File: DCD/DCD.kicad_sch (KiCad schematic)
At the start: 0 parts

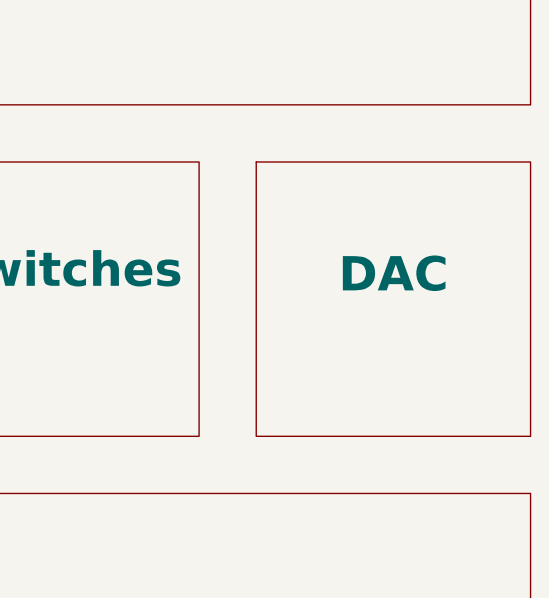
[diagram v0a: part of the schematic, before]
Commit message: DAC schematic with opamp and top level added
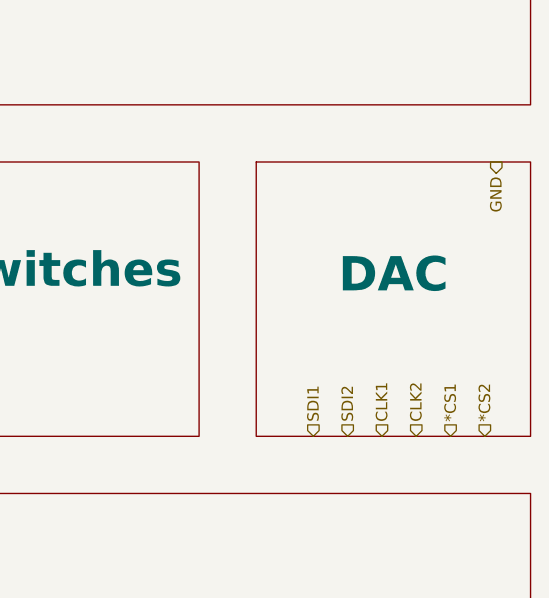
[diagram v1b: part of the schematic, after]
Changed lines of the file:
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@@
 	(generator_version "9.0")
 	(paper "A4")
+	(hierarchical_label "*CS2"
+		(shape input)
+		(at 177.8 109.22 90)
+		(effects
+			(font
+				(size 1.27 1.27)
+			)
+			(justify left)
+		)
+	)
+	(hierarchical_label "CLK2"
+		(shape input)
+		(at 170.18 109.22 90)
+		(effects
+			(font
+				(size 1.27 1.27)
+			)
+			(justify left)
+		)
+	)
+	(hierarchical_label "CLK1"
+		(shape input)
+		(at 166.37 109.22 90)
+		(effects
+			(font
+				(size 1.27 1.27)
+			)
+			(justify left)
+		)
+	)
+	(hierarchical_label "SDI1"
+		(shape input)
+		(at 158.75 109.22 90)
+		(effects
+			(font
+				(size 1.27 1.27)
+			)
+			(justify left)
+		)
+	)
+	(hierarchical_label "GND"
+		(shape output)
+		(at 179.07 78.74 270)
+		(effects
+			(font
+				(size 1.27 1.27)
+			)
+			(justify right)
+		)
+	)
+	(hierarchical_label "*CS1"
+		(shape input)
+		(at 173.99 109.22 90)
+		(effects
+			(font
+				(size 1.27 1.27)
+			)
+			(justify left)
+		)
+	)
+	(hierarchical_label "SDI2"
+		(shape input)
+		(at 162.56 109.22 90)
+		(effects
+			(font
+				(size 1.27 1.27)
+			)
+			(justify left)
+		)
+	)
 	(sheet
 		(at 152.4 78.74)

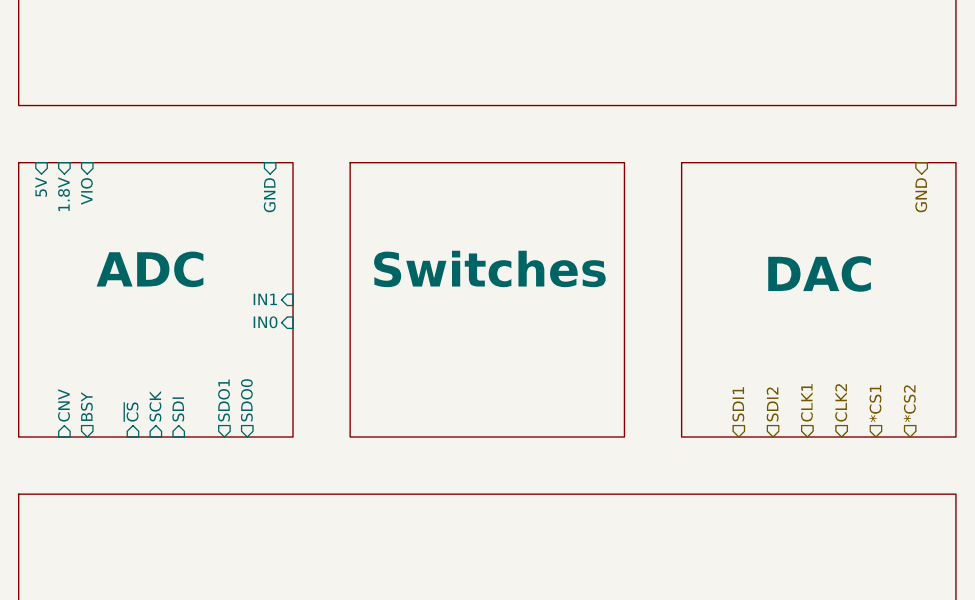
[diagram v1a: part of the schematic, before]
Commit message: Did the signal switching, finished ADC, misc changes to top
Decided to go with solder jumpers instead of power switches bc power
switches have no specs of linearity and they would add unnecessary
complexity, development time, and routing problems.

The calibration test has to be done only once and the chamber doesn't
even have to be sealed for it, so it shouldn't add too much hassle.
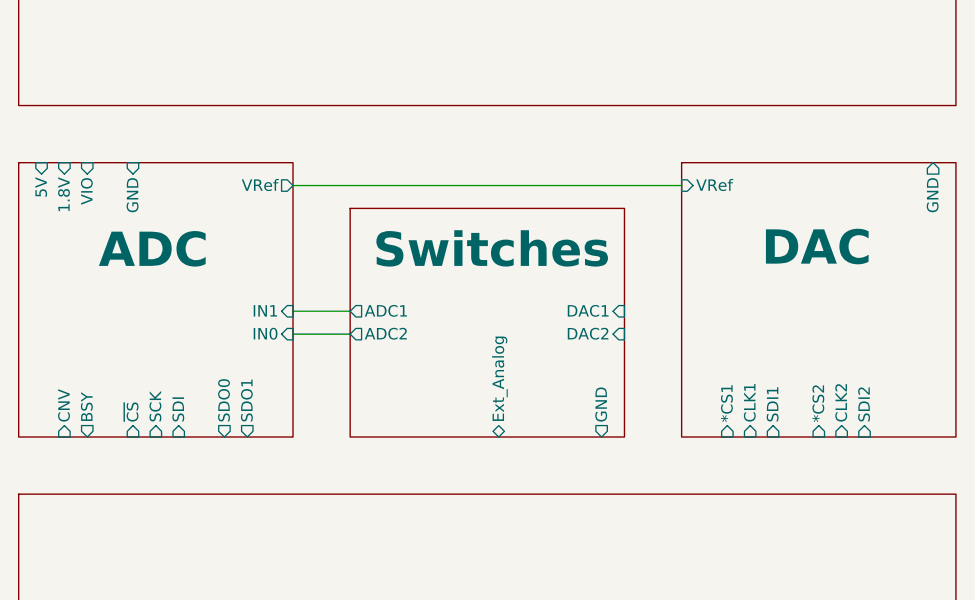
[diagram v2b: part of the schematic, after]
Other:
- sheet ADC ports: added VRef; removed none
- sheet DAC ports: added *CS1, *CS2, CLK1, CLK2, GND, SDI1, SDI2, VRef; removed none
- sheet Switches ports: added ADC1, ADC2, DAC1, DAC2, Ext_Analog, GND; removed none
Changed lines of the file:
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@@
 	(generator_version "9.0")
 	(paper "A4")
-	(hierarchical_label "*CS2"
-		(shape input)
-		(at 177.8 109.22 90)
-		(effects
-			(font
-				(size 1.27 1.27)
-			)
-			(justify left)
-		)
-	)
-	(hierarchical_label "CLK2"
-		(shape input)
-		(at 170.18 109.22 90)
-		(effects
-			(font
-				(size 1.27 1.27)
-			)
-			(justify left)
-		)
-	)
-	(hierarchical_label "CLK1"
-		(shape input)
-		(at 166.37 109.22 90)
-		(effects
-			(font
-				(size 1.27 1.27)
-			)
-			(justify left)
-		)
-	)
-	(hierarchical_label "SDI1"
-		(shape input)
-		(at 158.75 109.22 90)
-		(effects
-			(font
-				(size 1.27 1.27)
-			)
-			(justify left)
-		)
-	)
-	(hierarchical_label "GND"
-		(shape output)
-		(at 179.07 78.74 270)
-		(effects
-			(font
-				(size 1.27 1.27)
-			)
-			(justify right)
-		)
-	)
-	(hierarchical_label "*CS1"
-		(shape input)
-		(at 173.99 109.22 90)
-		(effects
-			(font
-				(size 1.27 1.27)
-			)
-			(justify left)
-		)
-	)
-	(hierarchical_label "SDI2"
-		(shape input)
-		(at 162.56 109.22 90)
-		(effects
-			(font
-				(size 1.27 1.27)
-			)
-			(justify left)
+	(wire
+		(pts
+			(xy 109.22 81.28) (xy 152.4 81.28)
+		)
+		(stroke
+			(width 0)
+			(type default)
+		)
+	)
+	(wire
+		(pts
+			(xy 109.22 97.79) (xy 115.57 97.79)
+		)
+		(stroke
+			(width 0)
+			(type default)
+		)
+	)
+	(wire
+		(pts
+			(xy 109.22 95.25) (xy 115.57 95.25)
+		)
+		(stroke
+			(width 0)
+			(type default)
 		)
 	)
@@
 		)
 		(property "Sheetname" "DAC"
-			(at 161.544 93.472 0)
+			(at 161.29 90.424 0)
 			(effects
 				(font
@@
 				(justify left top)
 				(hide yes)
+			)
+		)
+		(pin "CLK1" input
+			(at 160.02 109.22 270)
+			(effects
+				(font
+					(size 1.27 1.27)
+				)
+				(justify left)
+			)
+		)
+		(pin "*CS2" input
+			(at 167.64 109.22 270)
+			(effects
+				(font
+					(size 1.27 1.27)
+				)
+				(justify left)
+			)
+		)
+		(pin "SDI2" input
+			(at 172.72 109.22 270)
+			(effects
+				(font
+					(size 1.27 1.27)
+				)
+				(justify left)
+			)
+		)
+		(pin "GND" output
+			(at 180.34 78.74 90)
+			(effects
+				(font
+					(size 1.27 1.27)
+				)
+				(justify right)
+			)
+		)
+		(pin "*CS1" input
+			(at 157.48 109.22 270)
+			(effects
+				(font
+					(size 1.27 1.27)
+				)
+				(justify left)
+			)
+		)
+		(pin "SDI1" input
+			(at 162.56 109.22 270)
+			(effects
+				(font
+					(size 1.27 1.27)
+				)
+				(justify left)
+			)
+		)
+		(pin "CLK2" input
+			(at 170.18 109.22 270)
+			(effects
+				(font
+					(size 1.27 1.27)
+				)
+				(justify left)
+			)
+		)
+		(pin "VRef" input
+			(at 152.4 81.28 180)
+			(effects
+				(font
+					(size 1.27 1.27)
+				)
+				(justify left)
 			)
 		)
@@
 	)
 	(sheet
-		(at 115.57 78.74)
-		(size 30.48 30.48)
+		(at 115.57 83.82)
+		(size 30.48 25.4)
 		(exclude_from_sim no)
 		(in_bom yes)
@@
 		)
 		(property "Sheetname" "Switches"
-			(at 117.856 92.964 0)
+			(at 118.11 90.678 0)
 			(effects
 				(font
@@
 		)
 		(property "Sheetfile" "Subcircuits/switches.kicad_sch"
-			(at 115.57 109.8046 0)
+			(at 115.57 114.8846 0)
 			(effects
 				(font
@@
 				(justify left top)
 				(hide yes)
+			)
+		)
+		(pin "GND" output
+			(at 143.51 109.22 270)
+			(effects
+				(font
+					(size 1.27 1.27)
+				)
+				(justify left)
+			)
+		)
+		(pin "Ext_Analog" bidirectional
+			(at 132.08 109.22 270)
+			(effects
+				(font
+					(size 1.27 1.27)
+				)
+				(justify left)
+			)
+		)
+		(pin "ADC1" output
+			(at 115.57 95.25 180)
+			(effects
+				(font
+					(size 1.27 1.27)
+				)
+				(justify left)
+			)
+		)
+		(pin "ADC2" output
+			(at 115.57 97.79 180)
+			(effects
+				(font
+					(size 1.27 1.27)
+				)
+				(justify left)
+			)
+		)
+		(pin "DAC2" input
+			(at 146.05 97.79 0)
+			(effects
+				(font
+					(size 1.27 1.27)
+				)
+				(justify right)
+			)
+		)
+		(pin "DAC1" input
+			(at 146.05 95.25 0)
+			(effects
+				(font
+					(size 1.27 1.27)
+				)
+				(justify right)
 			)
 		)
@@
 		)
 		(property "Sheetname" "ADC"
-			(at 87.376 92.964 0)
+			(at 87.63 90.678 0)
 			(effects
 				(font
@@
 		)
 		(pin "SDO1" output
-			(at 101.6 109.22 270)
+			(at 104.14 109.22 270)
 			(effects
 				(font
@@
 		)
 		(pin "SDO0" output
-			(at 104.14 109.22 270)
+			(at 101.6 109.22 270)
 			(effects
 				(font
@@
 		)
 		(pin "GND" input
-			(at 106.68 78.74 90)
+			(at 91.44 78.74 90)
 			(effects
 				(font
@@
 		)
 		(pin "IN1" input
-			(at 109.22 93.98 0)
+			(at 109.22 95.25 0)
 			(effects
 				(font
@@
 		)
 		(pin "IN0" input
-			(at 109.22 96.52 0)
+			(at 109.22 97.79 0)
 			(effects
 				(font
@@
 			(effects
 				(font
+					(size 1.27 1.27)
+				)
+				(justify right)
+			)
+		)
+		(pin "VRef" output
+			(at 109.22 81.28 0)
+			(effects
+				(font

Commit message: DAC design done and added component potentiometer
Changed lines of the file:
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@@
+		)
+	)
+	(hierarchical_label "VDD(3.3V)"
+		(shape input)
+		(at 175.26 78.74 270)
+		(effects
+			(font
+				(size 1.27 1.27)
+			)
+			(justify right)
 		)
 	)

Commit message: Added PSUS, progress on the PSU circuit design, slight tweaks to the rest
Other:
- sheet DAC ports: added VDD(3.3V); removed none
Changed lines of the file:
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@@
-		)
-	)
-	(hierarchical_label "VDD(3.3V)"
-		(shape input)
-		(at 175.26 78.74 270)
-		(effects
-			(font
-				(size 1.27 1.27)
-			)
-			(justify right)
 		)
 	)
@@
 		)
 		(pin "*CS2" input
-			(at 167.64 109.22 270)
+			(at 172.72 109.22 270)
 			(effects
 				(font
@@
 		)
 		(pin "SDI2" input
-			(at 172.72 109.22 270)
+			(at 177.8 109.22 270)
 			(effects
 				(font
@@
 		)
 		(pin "CLK2" input
-			(at 170.18 109.22 270)
+			(at 175.26 109.22 270)
 			(effects
 				(font
@@
 			)
 		)
+		(pin "VDD(3.3V)" input
+			(at 176.53 78.74 90)
+			(effects
+				(font
+					(size 1.27 1.27)
+				)
+				(justify right)
+			)
+		)

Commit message: Progress on the implementation of the DAC driver
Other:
- sheet ADC ports: added none; removed IN0, IN1
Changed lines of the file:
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@@
-			)
-		)
-		(pin "IN1" input
-			(at 109.22 95.25 0)
-			(effects
-				(font
-					(size 1.27 1.27)
-				)
-				(justify right)
 			)
 		)
@@
 			(effects
 				(font
-					(size 1.27 1.27)
-				)
-				(justify right)
-			)
-		)
-		(pin "IN0" input
-			(at 109.22 97.79 0)
-			(effects
-				(font

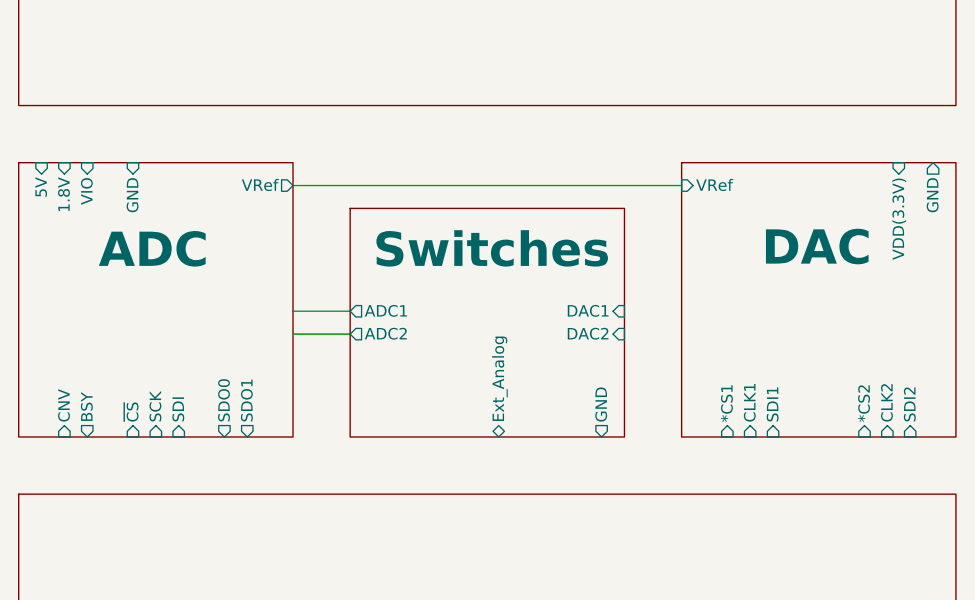
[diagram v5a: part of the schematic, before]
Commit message: Fixed the switches, finished the adc amplifier, missing the filer to adc
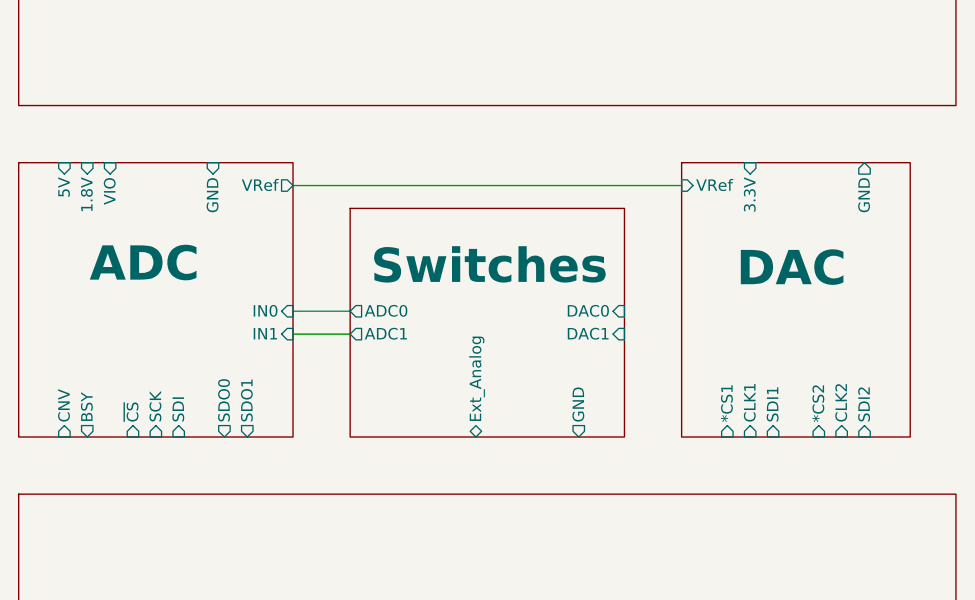
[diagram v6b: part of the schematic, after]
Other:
- sheet ADC ports: added IN0, IN1; removed none
- sheet DAC ports: added 3.3V; removed VDD(3.3V)
- sheet Switches ports: added ADC0, DAC0; removed ADC2, DAC2
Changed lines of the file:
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@@
+	(wire
+		(pts
+			(xy 109.22 95.25) (xy 115.57 95.25)
+		)
+		(stroke
+			(width 0)
+			(type default)
+		)
+	)
 	(wire
 		(pts
@@
 		)
 	)
-	(wire
-		(pts
-			(xy 109.22 95.25) (xy 115.57 95.25)
-		)
-		(stroke
-			(width 0)
-			(type default)
-		)
-	)
 	(sheet
 		(at 152.4 78.74)
-		(size 30.48 30.48)
+		(size 25.4 30.48)
 		(exclude_from_sim no)
 		(in_bom yes)
@@
 		)
 		(property "Sheetname" "DAC"
-			(at 161.29 90.424 0)
+			(at 158.496 92.71 0)
 			(effects
 				(font
@@
 		)
 		(pin "*CS2" input
+			(at 167.64 109.22 270)
+			(effects
+				(font
+					(size 1.27 1.27)
+				)
+				(justify left)
+			)
+		)
+		(pin "SDI2" input
 			(at 172.72 109.22 270)
 			(effects
@@
 			)
 		)
-		(pin "SDI2" input
-			(at 177.8 109.22 270)
-			(effects
-				(font
-					(size 1.27 1.27)
-				)
-				(justify left)
-			)
-		)
 		(pin "GND" output
-			(at 180.34 78.74 90)
+			(at 172.72 78.74 90)
 			(effects
 				(font
@@
 		)
 		(pin "CLK2" input
-			(at 175.26 109.22 270)
+			(at 170.18 109.22 270)
 			(effects
 				(font
@@
 			)
 		)
-		(pin "VDD(3.3V)" input
-			(at 176.53 78.74 90)
+		(pin "3.3V" input
+			(at 160.02 78.74 90)
 			(effects
 				(font
@@
 		)
 		(property "Sheetname" "Switches"
-			(at 118.11 90.678 0)
+			(at 117.856 92.456 0)
 			(effects
 				(font
@@
 		)
 		(pin "GND" output
-			(at 143.51 109.22 270)
+			(at 140.97 109.22 270)
+			(effects
+				(font
+					(size 1.27 1.27)
+				)
+				(justify left)
+			)
+		)
+		(pin "DAC1" input
+			(at 146.05 97.79 0)
+			(effects
+				(font
+					(size 1.27 1.27)
+				)
+				(justify right)
+			)
+		)
+		(pin "DAC0" input
+			(at 146.05 95.25 0)
+			(effects
+				(font
+					(size 1.27 1.27)
+				)
+				(justify right)
+			)
+		)
+		(pin "ADC0" output
+			(at 115.57 95.25 180)
 			(effects
 				(font
@@
 		)
 		(pin "Ext_Analog" bidirectional
-			(at 132.08 109.22 270)
+			(at 129.54 109.22 270)
 			(effects
 				(font
@@
 		)
 		(pin "ADC1" output
-			(at 115.57 95.25 180)
-			(effects
-				(font
-					(size 1.27 1.27)
-				)
-				(justify left)
-			)
-		)
-		(pin "ADC2" output
 			(at 115.57 97.79 180)
 			(effects
@@
 				)
 				(justify left)
-			)
-		)
-		(pin "DAC2" input
-			(at 146.05 97.79 0)
-			(effects
-				(font
-					(size 1.27 1.27)
-				)
-				(justify right)
-			)
-		)
-		(pin "DAC1" input
-			(at 146.05 95.25 0)
-			(effects
-				(font
-					(size 1.27 1.27)
-				)
-				(justify right)
 			)
 		)
@@
 		)
 		(property "Sheetname" "ADC"
-			(at 87.63 90.678 0)
+			(at 86.614 92.202 0)
 			(effects
 				(font
@@
 		)
 		(pin "5V" input
-			(at 81.28 78.74 90)
+			(at 83.82 78.74 90)
 			(effects
 				(font
@@
 		)
 		(pin "GND" input
-			(at 91.44 78.74 90)
+			(at 100.33 78.74 90)
 			(effects
 				(font
@@
 		)
 		(pin "1.8V" input
-			(at 83.82 78.74 90)
+			(at 86.36 78.74 90)
 			(effects
 				(font
@@
 		)
 		(pin "VIO" input
-			(at 86.36 78.74 90)
+			(at 88.9 78.74 90)
 			(effects
 				(font
@@
 			(effects
 				(font
+					(size 1.27 1.27)
+				)
+				(justify right)
+			)
+		)
+		(pin "IN0" input
+			(at 109.22 95.25 0)
+			(effects
+				(font
+					(size 1.27 1.27)
+				)
+				(justify right)
+			)
+		)
+		(pin "IN1" input
+			(at 109.22 97.79 0)
+			(effects
+				(font

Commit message: Finished the schematics. Fixed the comments that we recieved
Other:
- sheet Comms ports: added *CS1, *CS2, BSY, CLK, CNV, Ext, GND, SCK, SDI, SDI1, SDI2, SDO0, SDO1, VRef, Vin, ~{CS}; removed none
- sheet DAC ports: added DAC0, DAC1, VRef_Ext; removed none
- sheet PSUs ports: added 1.8V, 3.3V, 5V, GND, VIO, Vin; removed none
